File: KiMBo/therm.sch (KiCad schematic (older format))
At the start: 12 parts

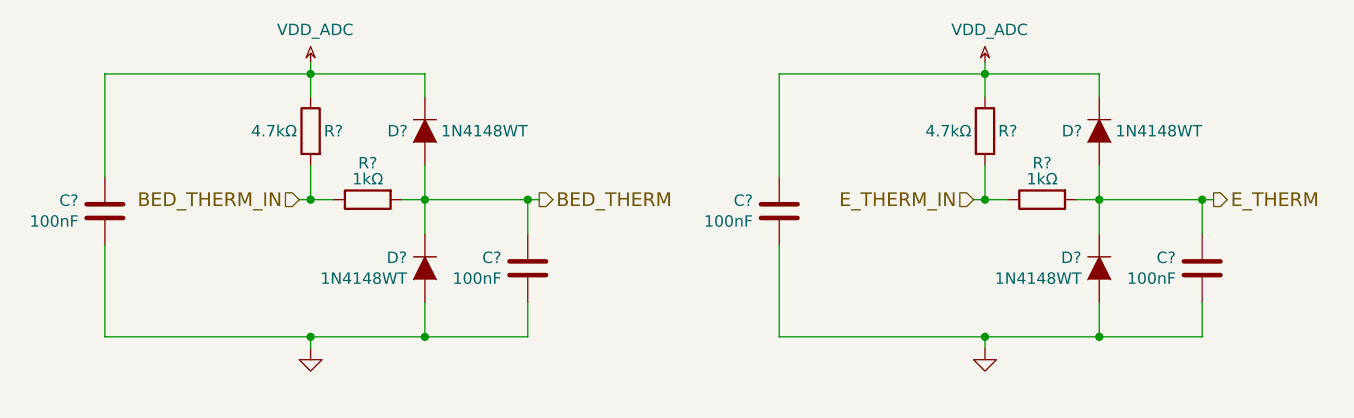
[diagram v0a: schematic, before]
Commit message: Add low pass filters to the outputs going to the heaters, fans, and to the endstop inputs.
The values of the passives need to be tweaked.
Ferrites need to be placed in series with the output to the heaters and fans.
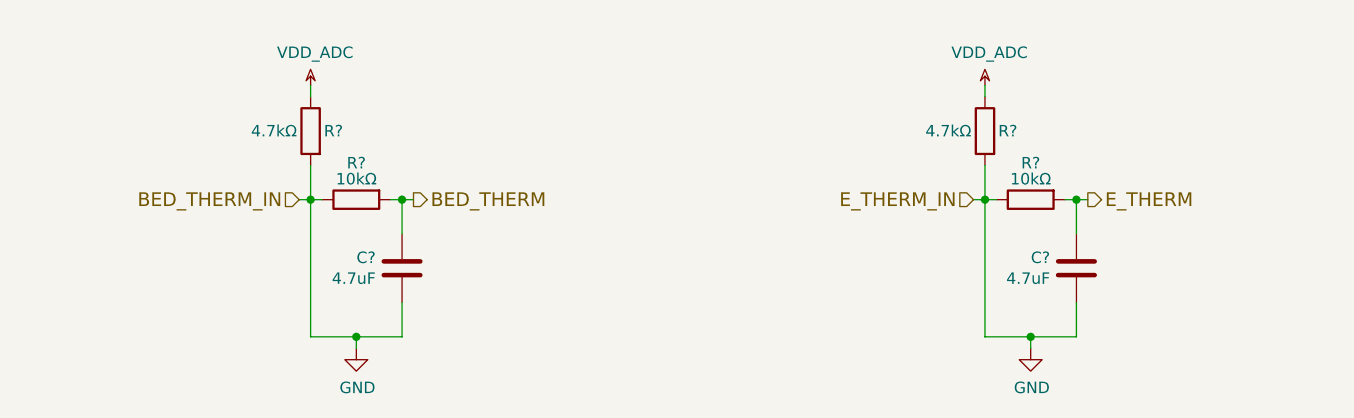
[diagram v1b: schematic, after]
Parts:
- removed C? (x2): 100nF, symbol C
- removed D? (x4): 1N4148WT, symbol D
- C? (x2): value 100nF -> 4.7uF
- R? (x2): value 1kΩ -> 10kΩ
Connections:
- net BED_THERM_IN is gone; now on net GND: R?.1, R?.2
- net E_THERM_IN is gone; now on net GND: R?.1, R?.2
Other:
- moved on the sheet: C?, R?

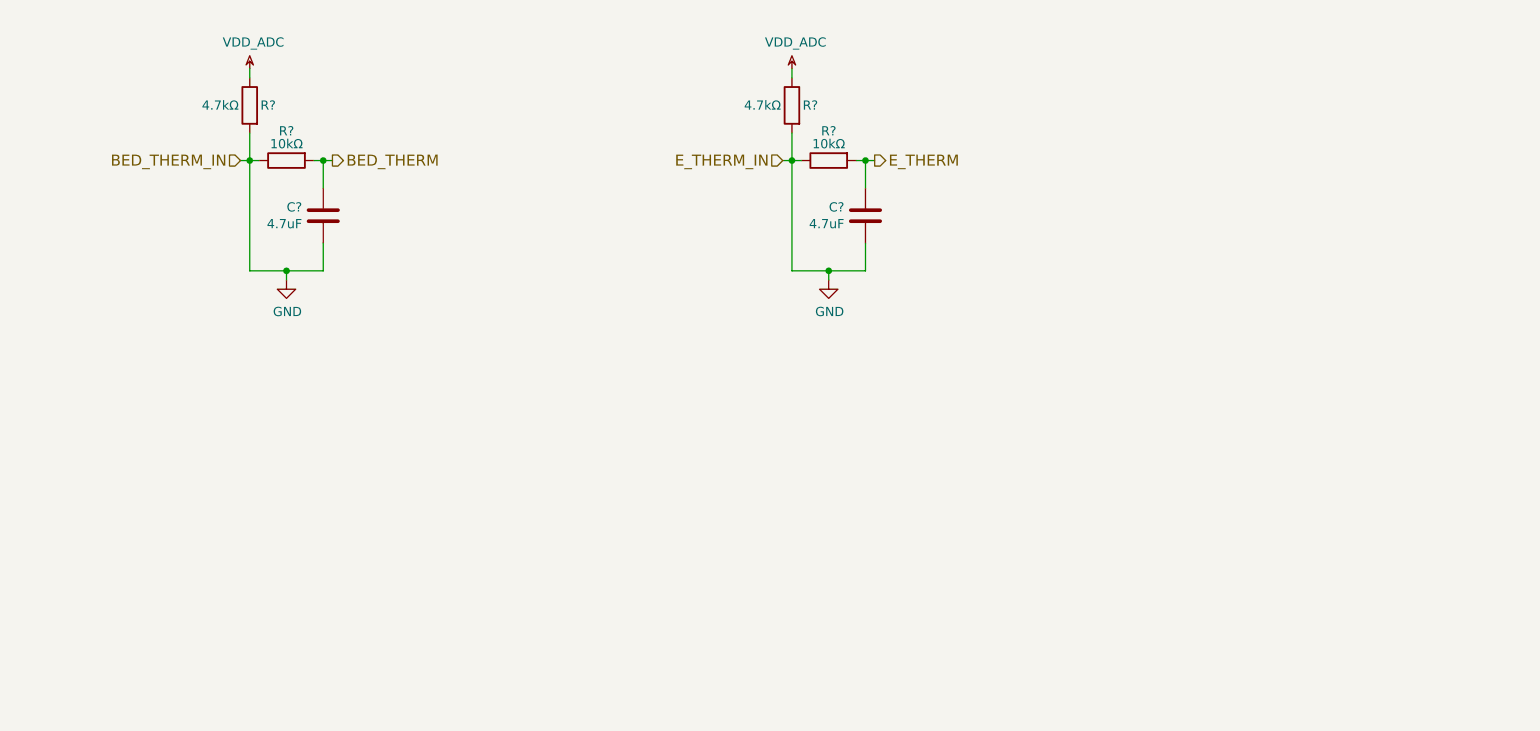
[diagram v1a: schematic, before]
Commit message: Update ferrite values, select fuse based on interrupt rating
The PSU needs to be able to supply at LEAST 25A to blow the fuse
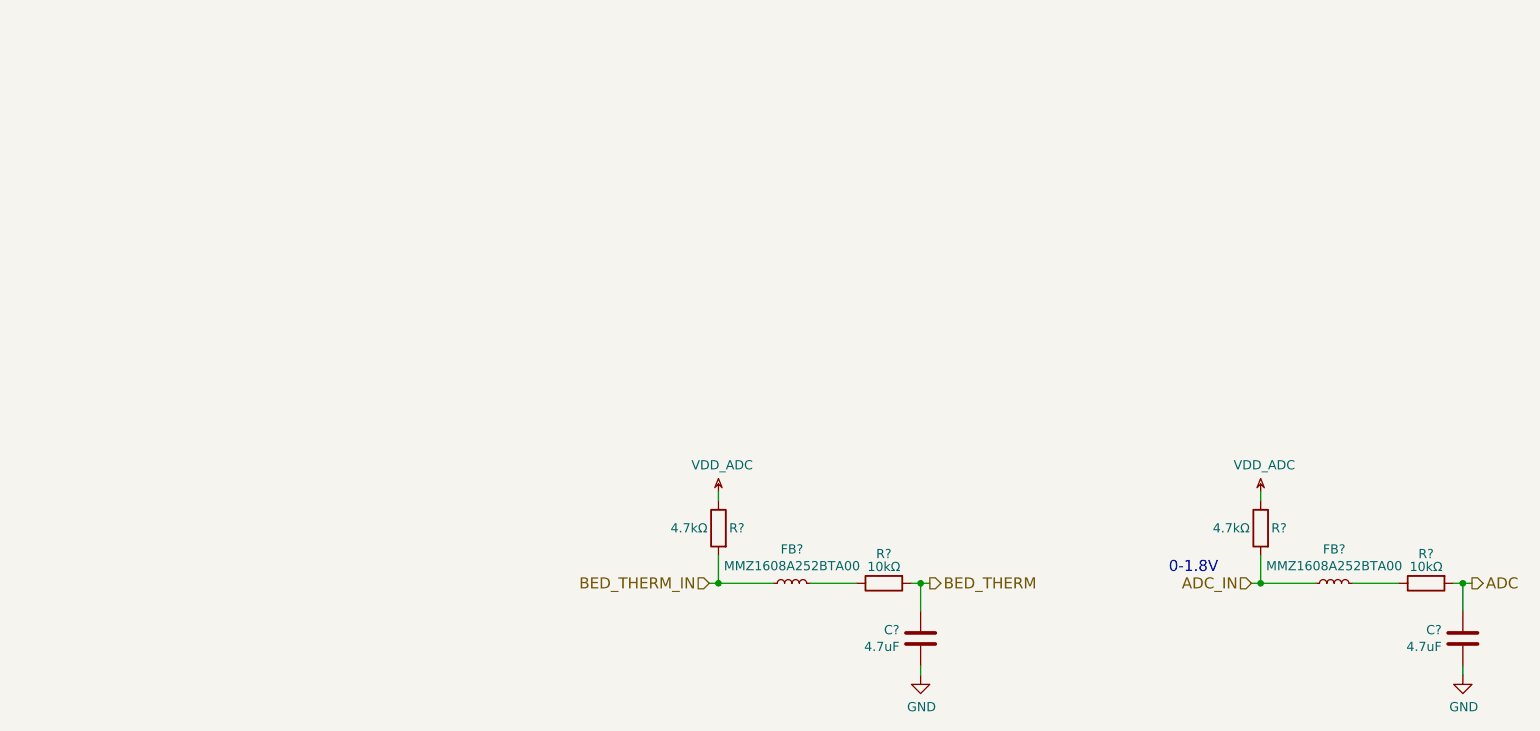
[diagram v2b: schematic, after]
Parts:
- added FB? (x2): MMZ1608A252BTA00, symbol INDUCTOR_Small
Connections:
- net GND: no longer R?.1, R?.1, R?.2, R?.2
- net E_THERM renamed ADC
- new net: FB?.2, R?.1 (x2)
- new net ADC_IN: FB?.1, R?.2
- new net BED_THERM_IN: FB?.1, R?.2
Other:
- note added: "0-1.8V"
- moved on the sheet: C?, R?
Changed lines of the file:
@@
 L C C?
 U 1 1 57931608
-P 3650 3250
-F 0 "C?" H 3535 3204 50  0000 R CNN
-F 1 "4.7uF" H 3535 3295 50  0000 R CNN
-F 2 "" H 3688 3100 50  0000 C CNN
-F 3 "" H 3650 3250 50  0000 C CNN
-	1    3650 3250
+P 6900 5550
+F 0 "C?" H 6785 5504 50  0000 R CNN
+F 1 "4.7uF" H 6785 5595 50  0000 R CNN
+F 2 "" H 6938 5400 50  0000 C CNN
+F 3 "" H 6900 5550 50  0000 C CNN
+	1    6900 5550
 	1    0    0    1
 $EndComp
@@
 L R R?
 U 1 1 57931779
-P 3450 2950
-F 0 "R?" V 3290 2950 50  0000 C CNN
-F 1 "10kΩ" V 3360 2950 50  0000 C CNN
-F 2 "" V 3380 2950 50  0000 C CNN
-F 3 "" H 3450 2950 50  0000 C CNN
-	1    3450 2950
+P 6700 5250
+F 0 "R?" V 6540 5250 50  0000 C CNN
+F 1 "10kΩ" V 6610 5250 50  0000 C CNN
+F 2 "" V 6630 5250 50  0000 C CNN
+F 3 "" H 6700 5250 50  0000 C CNN
+	1    6700 5250
 	0    -1   1    0
 $EndComp
@@
 L R R?
 U 1 1 57931815
-P 3250 2650
-F 0 "R?" H 3150 2650 50  0000 C CNN
-F 1 "4.7kΩ" H 3410 2650 50  0000 C CNN
-F 2 "" V 3180 2650 50  0000 C CNN
-F 3 "" H 3250 2650 50  0000 C CNN
-	1    3250 2650
+P 5800 4950
+F 0 "R?" H 5700 4950 50  0000 C CNN
+F 1 "4.7kΩ" H 5960 4950 50  0000 C CNN
+F 2 "" V 5730 4950 50  0000 C CNN
+F 3 "" H 5800 4950 50  0000 C CNN
+	1    5800 4950
 	-1   0    0    -1
 $EndComp
-Text HLabel 3700 2950 2    60   Output ~ 0
+Text HLabel 6950 5250 2    60   Output ~ 0
 BED_THERM
-Text HLabel 3200 2950 0    60   Input ~ 0
+Text HLabel 5750 5250 0    60   Input ~ 0
 BED_THERM_IN
 $Comp
 L VDD_ADC #PWR?
 U 1 1 59E74D42
-P 3250 2450
-F 0 "#PWR?" H 3400 2400 50  0001 C CNN
-F 1 "VDD_ADC" H 3270 2593 50  0000 C CNN
-F 2 "" H 3250 2450 50  0000 C CNN
-F 3 "" H 3250 2450 50  0000 C CNN
-	1    3250 2450
+P 5800 4750
+F 0 "#PWR?" H 5950 4700 50  0001 C CNN
+F 1 "VDD_ADC" H 5820 4893 50  0000 C CNN
+F 2 "" H 5800 4750 50  0000 C CNN
+F 3 "" H 5800 4750 50  0000 C CNN
+	1    5800 4750
 	1    0    0    -1
 $EndComp
@@
 L C C?
 U 1 1 5AD7EE6B
-P 6600 3250
-F 0 "C?" H 6485 3204 50  0000 R CNN
-F 1 "4.7uF" H 6485 3295 50  0000 R CNN
-F 2 "" H 6638 3100 50  0000 C CNN
-F 3 "" H 6600 3250 50  0000 C CNN
-	1    6600 3250
+P 9850 5550
+F 0 "C?" H 9735 5504 50  0000 R CNN
+F 1 "4.7uF" H 9735 5595 50  0000 R CNN
+F 2 "" H 9888 5400 50  0000 C CNN
+F 3 "" H 9850 5550 50  0000 C CNN
+	1    9850 5550
 	1    0    0    1
 $EndComp
@@
 L R R?
 U 1 1 5AD7EE80
-P 6400 2950
-F 0 "R?" V 6240 2950 50  0000 C CNN
-F 1 "10kΩ" V 6310 2950 50  0000 C CNN
-F 2 "" V 6330 2950 50  0000 C CNN
-F 3 "" H 6400 2950 50  0000 C CNN
-	1    6400 2950
+P 9650 5250
+F 0 "R?" V 9490 5250 50  0000 C CNN
+F 1 "10kΩ" V 9560 5250 50  0000 C CNN
+F 2 "" V 9580 5250 50  0000 C CNN
+F 3 "" H 9650 5250 50  0000 C CNN
+	1    9650 5250
 	0    -1   1    0
 $EndComp
@@
 L R R?
 U 1 1 5AD7EE87
-P 6200 2650
-F 0 "R?" H 6100 2650 50  0000 C CNN
-F 1 "4.7kΩ" H 6360 2650 50  0000 C CNN
-F 2 "" V 6130 2650 50  0000 C CNN
-F 3 "" H 6200 2650 50  0000 C CNN
-	1    6200 2650
+P 8750 4950
+F 0 "R?" H 8650 4950 50  0000 C CNN
+F 1 "4.7kΩ" H 8910 4950 50  0000 C CNN
+F 2 "" V 8680 4950 50  0000 C CNN
+F 3 "" H 8750 4950 50  0000 C CNN
+	1    8750 4950
 	-1   0    0    -1
 $EndComp
-Text HLabel 6650 2950 2    60   Output ~ 0
-E_THERM
-Text HLabel 6150 2950 0    60   Input ~ 0
-E_THERM_IN
+Text HLabel 9900 5250 2    60   Output ~ 0
+ADC
+Text HLabel 8700 5250 0    60   Input ~ 0
+ADC_IN
 $Comp
 L VDD_ADC #PWR?
 U 1 1 5AD7EEB1
-P 6200 2450
-F 0 "#PWR?" H 6350 2400 50  0001 C CNN
-F 1 "VDD_ADC" H 6220 2593 50  0000 C CNN
-F 2 "" H 6200 2450 50  0000 C CNN
-F 3 "" H 6200 2450 50  0000 C CNN
-	1    6200 2450
+P 8750 4750
+F 0 "#PWR?" H 8900 4700 50  0001 C CNN
+F 1 "VDD_ADC" H 8770 4893 50  0000 C CNN
+F 2 "" H 8750 4750 50  0000 C CNN
+F 3 "" H 8750 4750 50  0000 C CNN
+	1    8750 4750
 	1    0    0    -1
 $EndComp
-Connection ~ 6200 2950
-Connection ~ 6400 3550
-Wire Wire Line
-	6600 3550 6600 3400
-Connection ~ 6600 2950
-Wire Wire Line
-	6600 2950 6600 3100
-Wire Wire Line
-	6150 2950 6200 2950
-Wire Wire Line
-	6200 2950 6250 2950
-Wire Wire Line
-	6550 2950 6600 2950
-Wire Wire Line
-	6600 2950 6650 2950
-Wire Wire Line
-	3250 2800 3250 2950
-Wire Wire Line
-	3250 2950 3250 3550
-Connection ~ 3250 2950
-Connection ~ 3450 3550
-Wire Wire Line
-	3650 3550 3650 3400
-Connection ~ 3650 2950
-Wire Wire Line
-	3650 2950 3650 3100
-Wire Wire Line
-	3200 2950 3250 2950
-Wire Wire Line
-	3250 2950 3300 2950
-Wire Wire Line
-	6200 3550 6400 3550
-Wire Wire Line
-	6400 3550 6600 3550
-Wire Wire Line
-	3250 3550 3450 3550
-Wire Wire Line
-	3450 3550 3650 3550
 $Comp
 L GND #PWR?
 U 1 1 5B331170
-P 3450 3600
-F 0 "#PWR?" H 3450 3350 50  0001 C CNN
-F 1 "GND" H 3455 3427 50  0000 C CNN
-F 2 "" H 3450 3600 50  0000 C CNN
-F 3 "" H 3450 3600 50  0000 C CNN
-	1    3450 3600
+P 6900 5750
+F 0 "#PWR?" H 6900 5500 50  0001 C CNN
+F 1 "GND" H 6905 5577 50  0000 C CNN
+F 2 "" H 6900 5750 50  0000 C CNN
+F 3 "" H 6900 5750 50  0000 C CNN
+	1    6900 5750
 	1    0    0    -1
 $EndComp
@@
 L GND #PWR?
 U 1 1 5B3311A0
-P 6400 3600
-F 0 "#PWR?" H 6400 3350 50  0001 C CNN
-F 1 "GND" H 6405 3427 50  0000 C CNN
-F 2 "" H 6400 3600 50  0000 C CNN
-F 3 "" H 6400 3600 50  0000 C CNN
-	1    6400 3600
+P 9850 5750
+F 0 "#PWR?" H 9850 5500 50  0001 C CNN
+F 1 "GND" H 9855 5577 50  0000 C CNN
+F 2 "" H 9850 5750 50  0000 C CNN
+F 3 "" H 9850 5750 50  0000 C CNN
+	1    9850 5750
 	1    0    0    -1
 $EndComp
+$Comp
+L INDUCTOR_Small FB?
+U 1 1 5B885A27
+P 6200 5250
+F 0 "FB?" V 6385 5250 50  0000 C CNN
+F 1 "MMZ1608A252BTA00" V 6294 5250 50  0000 C CNN
+F 2 "" H 6200 5250 50  0000 C CNN
+F 3 "" H 6200 5250 50  0000 C CNN
+	1    6200 5250
+	0    -1   -1   0
+$EndComp
+Text Notes 8250 5200 0    60   ~ 0
+0-1.8V
 Wire Wire Line
-	6200 2800 6200 2950
+	9250 5250 9500 5250
 Wire Wire Line
-	6200 2950 6200 3550
+	6300 5250 6550 5250
 Wire Wire Line
-	6400 3550 6400 3600
+	8750 4750 8750 4800
 Wire Wire Line
-	3600 2950 3650 2950
+	5800 4750 5800 4800
 Wire Wire Line
-	3650 2950 3700 2950
+	6850 5250 6900 5250
 Wire Wire Line
-	3450 3550 3450 3600
+	6900 5250 6950 5250
 Wire Wire Line
-	3250 2450 3250 2500
+	5750 5250 5800 5250
 Wire Wire Line
-	6200 2450 6200 2500
+	5800 5250 6100 5250
+Wire Wire Line
+	6900 5250 6900 5400
+Connection ~ 6900 5250
+Wire Wire Line
+	6900 5750 6900 5700
+Connection ~ 5800 5250
+Wire Wire Line
+	5800 5100 5800 5250
+Wire Wire Line
+	9800 5250 9850 5250
+Wire Wire Line
+	9850 5250 9900 5250
+Wire Wire Line
+	8700 5250 8750 5250
+Wire Wire Line
+	8750 5250 9050 5250
+Wire Wire Line
+	9850 5250 9850 5400
+Connection ~ 9850 5250
+Wire Wire Line
+	9850 5750 9850 5700
+Connection ~ 8750 5250
+Wire Wire Line
+	8750 5250 8750 5100
+$Comp
+L INDUCTOR_Small FB?
+U 1 1 5B8FFD1D
+P 9150 5250
+F 0 "FB?" V 9335 5250 50  0000 C CNN
+F 1 "MMZ1608A252BTA00" V 9244 5250 50  0000 C CNN
+F 2 "" H 9150 5250 50  0000 C CNN
+F 3 "" H 9150 5250 50  0000 C CNN
+	1    9150 5250
+	0    -1   -1   0
+$EndComp
 $EndSCHEMATC

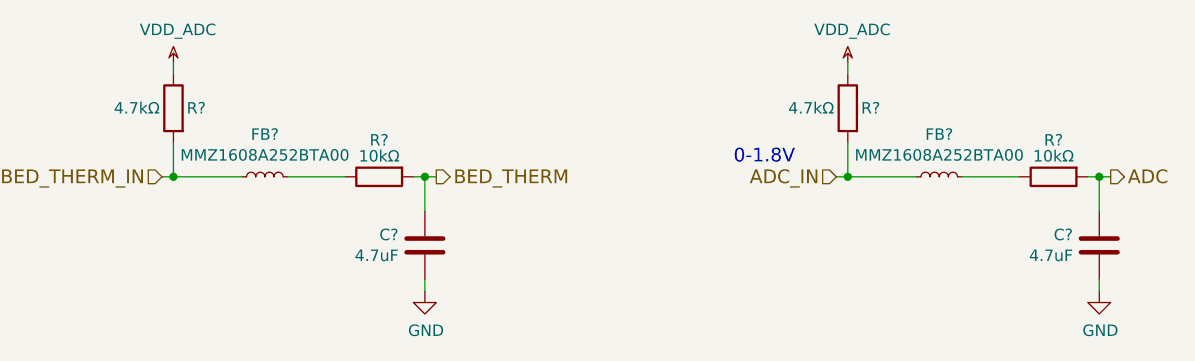
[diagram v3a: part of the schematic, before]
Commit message: Annotate all components, now passing ERC, added ferrites to the rest of the connectors
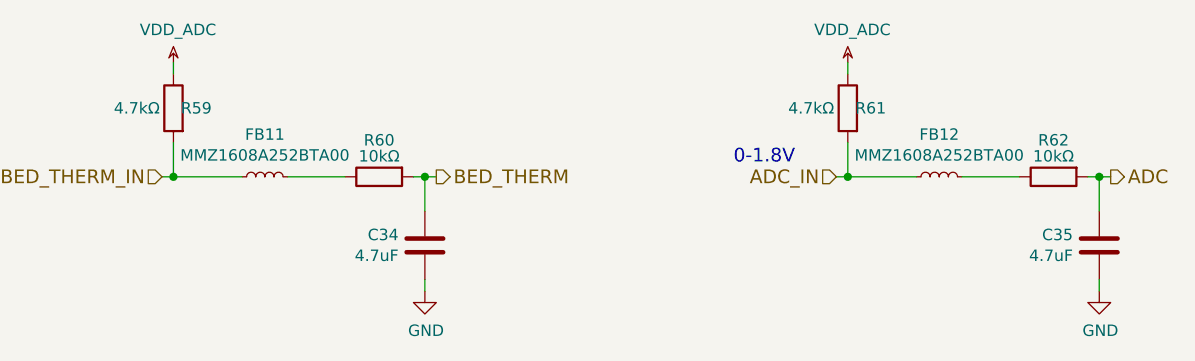
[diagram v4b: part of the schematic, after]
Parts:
- gave numbers to parts that had none: 8
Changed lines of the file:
@@
 $EndDescr
 $Comp
-L C C?
+L C C34
 U 1 1 57931608
 P 6900 5550
-F 0 "C?" H 6785 5504 50  0000 R CNN
+F 0 "C34" H 6785 5504 50  0000 R CNN
 F 1 "4.7uF" H 6785 5595 50  0000 R CNN
 F 2 "" H 6938 5400 50  0000 C CNN
@@
 $EndComp
 $Comp
-L R R?
+L R R60
 U 1 1 57931779
 P 6700 5250
-F 0 "R?" V 6540 5250 50  0000 C CNN
+F 0 "R60" V 6540 5250 50  0000 C CNN
 F 1 "10kΩ" V 6610 5250 50  0000 C CNN
 F 2 "" V 6630 5250 50  0000 C CNN
@@
 $EndComp
 $Comp
-L R R?
+L R R59
 U 1 1 57931815
 P 5800 4950
-F 0 "R?" H 5700 4950 50  0000 C CNN
+F 0 "R59" H 5700 4950 50  0000 C CNN
 F 1 "4.7kΩ" H 5960 4950 50  0000 C CNN
 F 2 "" V 5730 4950 50  0000 C CNN
@@
 BED_THERM_IN
 $Comp
-L VDD_ADC #PWR0127
+L VDD_ADC #PWR0175
 U 1 1 59E74D42
 P 5800 4750
-F 0 "#PWR0127" H 5950 4700 50  0001 C CNN
+F 0 "#PWR0175" H 5950 4700 50  0001 C CNN
 F 1 "VDD_ADC" H 5820 4893 50  0000 C CNN
 F 2 "" H 5800 4750 50  0000 C CNN
@@
 $EndComp
 $Comp
-L C C?
+L C C35
 U 1 1 5AD7EE6B
 P 9850 5550
-F 0 "C?" H 9735 5504 50  0000 R CNN
+F 0 "C35" H 9735 5504 50  0000 R CNN
 F 1 "4.7uF" H 9735 5595 50  0000 R CNN
 F 2 "" H 9888 5400 50  0000 C CNN
@@
 $EndComp
 $Comp
-L R R?
+L R R62
 U 1 1 5AD7EE80
 P 9650 5250
-F 0 "R?" V 9490 5250 50  0000 C CNN
+F 0 "R62" V 9490 5250 50  0000 C CNN
 F 1 "10kΩ" V 9560 5250 50  0000 C CNN
 F 2 "" V 9580 5250 50  0000 C CNN
@@
 $EndComp
 $Comp
-L R R?
+L R R61
 U 1 1 5AD7EE87
 P 8750 4950
-F 0 "R?" H 8650 4950 50  0000 C CNN
+F 0 "R61" H 8650 4950 50  0000 C CNN
 F 1 "4.7kΩ" H 8910 4950 50  0000 C CNN
 F 2 "" V 8680 4950 50  0000 C CNN
@@
 ADC_IN
 $Comp
-L VDD_ADC #PWR0128
+L VDD_ADC #PWR0176
 U 1 1 5AD7EEB1
 P 8750 4750
-F 0 "#PWR0128" H 8900 4700 50  0001 C CNN
+F 0 "#PWR0176" H 8900 4700 50  0001 C CNN
 F 1 "VDD_ADC" H 8770 4893 50  0000 C CNN
 F 2 "" H 8750 4750 50  0000 C CNN
@@
 $EndComp
 $Comp
-L GND #PWR0129
+L GND #PWR0177
 U 1 1 5B331170
 P 6900 5750
-F 0 "#PWR0129" H 6900 5500 50  0001 C CNN
+F 0 "#PWR0177" H 6900 5500 50  0001 C CNN
 F 1 "GND" H 6905 5577 50  0000 C CNN
 F 2 "" H 6900 5750 50  0000 C CNN
@@
 $EndComp
 $Comp
-L GND #PWR0130
+L GND #PWR0178
 U 1 1 5B3311A0
 P 9850 5750
-F 0 "#PWR0130" H 9850 5500 50  0001 C CNN
+F 0 "#PWR0178" H 9850 5500 50  0001 C CNN
 F 1 "GND" H 9855 5577 50  0000 C CNN
 F 2 "" H 9850 5750 50  0000 C CNN
@@
 $EndComp
 $Comp
-L INDUCTOR_Small FB?
+L INDUCTOR_Small FB11
 U 1 1 5B885A27
 P 6200 5250
-F 0 "FB?" V 6385 5250 50  0000 C CNN
+F 0 "FB11" V 6385 5250 50  0000 C CNN
 F 1 "MMZ1608A252BTA00" V 6294 5250 50  0000 C CNN
 F 2 "" H 6200 5250 50  0000 C CNN
@@
 	5800 4750 5800 4800
 Wire Wire Line
-	6850 5250 6900 5250
+	6850 5250 6950 5250
 Wire Wire Line
-	6900 5250 6950 5250
-Wire Wire Line
-	5750 5250 5800 5250
-Wire Wire Line
-	5800 5250 6100 5250
+	5750 5250 6100 5250
 Wire Wire Line
 	6900 5250 6900 5400
@@
 	5800 5100 5800 5250
 Wire Wire Line
-	9800 5250 9850 5250
+	9800 5250 9900 5250
 Wire Wire Line
-	9850 5250 9900 5250
-Wire Wire Line
-	8700 5250 8750 5250
-Wire Wire Line
-	8750 5250 9050 5250
+	8700 5250 9050 5250
 Wire Wire Line
 	9850 5250 9850 5400
@@
 	8750 5250 8750 5100
 $Comp
-L INDUCTOR_Small FB?
+L INDUCTOR_Small FB12
 U 1 1 5B8FFD1D
 P 9150 5250
-F 0 "FB?" V 9335 5250 50  0000 C CNN
+F 0 "FB12" V 9335 5250 50  0000 C CNN
 F 1 "MMZ1608A252BTA00" V 9244 5250 50  0000 C CNN
 F 2 "" H 9150 5250 50  0000 C CNN
